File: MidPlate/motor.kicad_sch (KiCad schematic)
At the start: 3 parts, among them J13 JST_BM04B-GHS-TBT, J7 430450818, J8 Molex_43045_8pinMicrofit

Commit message: midplate changes, ready for order
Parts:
- removed J8: Molex_43045_8pinMicrofit, bots:Molex_Micro-Fit_3.0_43045-0812_2x04_P3.00mm_Vertical, symbol bots:Molex_43045_8pinMicrofit
- added JP1: Jumper_2_Bridged, Connector_PinHeader_2.54mm:PinHeader_1x02_P2.54mm_Vertical, symbol Jumper:Jumper_2_Bridged
- added R3: R_110R, bots:R_0603_1608Metric, symbol bots:R_110R
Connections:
- net CAN+: now also R3.2
- net CAN-: now also JP1.1 (A)
- new net: JP1.2 (B), R3.1
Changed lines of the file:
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@@
 (kicad_sch (version 20230121) (generator eeschema)
   (paper "A4")
-  (junction (at 189.23 40.64) (diameter 0) (color 0 0 0 0)
-  )
   (junction (at 170.18 60.96) (diameter 0) (color 0 0 0 0)
   )
   (junction (at 195.58 66.04) (diameter 0) (color 0 0 0 0)
   )
+  (junction (at 118.11 110.49) (diameter 0) (color 0 0 0 0)
+  )
+  (junction (at 92.71 110.49) (diameter 0) (color 0 0 0 0)
+  )
   (junction (at 195.58 63.5) (diameter 0) (color 0 0 0 0)
   )
-  (junction (at 176.53 45.72) (diameter 0) (color 0 0 0 0)
-  )
-  (junction (at 176.53 43.18) (diameter 0) (color 0 0 0 0)
-  )
-  (junction (at 189.23 43.18) (diameter 0) (color 0 0 0 0)
-  )
-  (junction (at 176.53 40.64) (diameter 0) (color 0 0 0 0)
-  )
-  (junction (at 189.23 45.72) (diameter 0) (color 0 0 0 0)
-  )
   (junction (at 170.18 63.5) (diameter 0) (color 0 0 0 0)
   )
@@
     (stroke (width 0) (type default))
   )
-  (wire (pts (xy 189.23 52.07) (xy 195.58 52.07))
-    (stroke (width 0) (type default))
-  )
-  (wire (pts (xy 176.53 43.18) (xy 176.53 45.72))
-    (stroke (width 0) (type default))
-  )
   (wire (pts (xy 107.95 80.01) (xy 107.95 87.63))
     (stroke (width 0) (type default))
   )
-  (wire (pts (xy 170.18 53.34) (xy 170.18 60.96))
-    (stroke (width 0) (type default))
-  )
-  (wire (pts (xy 189.23 40.64) (xy 189.23 43.18))
-    (stroke (width 0) (type default))
-  )
-  (wire (pts (xy 176.53 40.64) (xy 176.53 43.18))
+  (wire (pts (xy 92.71 106.68) (xy 113.03 106.68))
+    (stroke (width 0) (type default))
+  )
+  (wire (pts (xy 105.41 110.49) (xy 107.95 110.49))
     (stroke (width 0) (type default))
   )
@@
     (stroke (width 0) (type default))
   )
+  (wire (pts (xy 92.71 106.68) (xy 92.71 110.49))
+    (stroke (width 0) (type default))
+  )
   (wire (pts (xy 161.29 68.58) (xy 161.29 60.96))
     (stroke (width 0) (type default))
@@
     (stroke (width 0) (type default))
   )
-  (wire (pts (xy 115.57 72.39) (xy 115.57 80.01))
-    (stroke (width 0) (type default))
-  )
-  (wire (pts (xy 176.53 53.34) (xy 170.18 53.34))
+  (wire (pts (xy 118.11 106.68) (xy 118.11 110.49))
+    (stroke (width 0) (type default))
+  )
+  (wire (pts (xy 118.11 110.49) (xy 127 110.49))
     (stroke (width 0) (type default))
   )
@@
     (stroke (width 0) (type default))
   )
+  (wire (pts (xy 115.57 106.68) (xy 115.57 72.39))
+    (stroke (width 0) (type default))
+  )
   (wire (pts (xy 170.18 63.5) (xy 170.18 66.04))
     (stroke (width 0) (type default))
   )
+  (wire (pts (xy 118.11 106.68) (xy 115.57 106.68))
+    (stroke (width 0) (type default))
+  )
   (wire (pts (xy 120.65 80.01) (xy 120.65 88.9))
     (stroke (width 0) (type default))
   )
-  (wire (pts (xy 195.58 52.07) (xy 195.58 60.96))
+  (wire (pts (xy 88.9 110.49) (xy 92.71 110.49))
+    (stroke (width 0) (type default))
+  )
+  (wire (pts (xy 92.71 110.49) (xy 95.25 110.49))
     (stroke (width 0) (type default))
   )
@@
     (stroke (width 0) (type default))
   )
-  (wire (pts (xy 113.03 72.39) (xy 113.03 80.01))
-    (stroke (width 0) (type default))
-  )
-  (wire (pts (xy 189.23 43.18) (xy 189.23 45.72))
+  (wire (pts (xy 115.57 110.49) (xy 118.11 110.49))
     (stroke (width 0) (type default))
   )
@@
     (stroke (width 0) (type default))
   )
+  (wire (pts (xy 88.9 113.03) (xy 88.9 110.49))
+    (stroke (width 0) (type default))
+  )
   (wire (pts (xy 195.58 66.04) (xy 195.58 68.58))
     (stroke (width 0) (type default))
@@
     (stroke (width 0) (type default))
   )
-  (wire (pts (xy 176.53 45.72) (xy 176.53 53.34))
-    (stroke (width 0) (type default))
-  )
-  (wire (pts (xy 189.23 45.72) (xy 189.23 52.07))
-    (stroke (width 0) (type default))
-  )
-  (wire (pts (xy 189.23 38.1) (xy 189.23 40.64))
-    (stroke (width 0) (type default))
-  )
-  (wire (pts (xy 176.53 38.1) (xy 176.53 40.64))
-    (stroke (width 0) (type default))
-  )
-  (global_label "CAN+" (shape input) (at 115.57 80.01 270) (fields_autoplaced)
+  (wire (pts (xy 113.03 106.68) (xy 113.03 72.39))
+    (stroke (width 0) (type default))
+  )
+  (global_label "CAN+" (shape input) (at 127 110.49 270) (fields_autoplaced)
     (effects (font (size 1.27 1.27)) (justify right))
-    (property "Intersheetrefs" "${INTERSHEET_REFS}" (at 115.57 88.2567 90)
+    (property "Intersheetrefs" "${INTERSHEET_REFS}" (at 127 118.7367 90)
       (effects (font (size 1.27 1.27)) (justify right) hide)
     )
   )
-  (global_label "CAN-" (shape input) (at 113.03 80.01 270) (fields_autoplaced)
+  (global_label "CAN-" (shape input) (at 88.9 113.03 270) (fields_autoplaced)
     (effects (font (size 1.27 1.27)) (justify right))
-    (property "Intersheetrefs" "${INTERSHEET_REFS}" (at 113.03 88.2567 90)
+    (property "Intersheetrefs" "${INTERSHEET_REFS}" (at 88.9 121.2767 90)
       (effects (font (size 1.27 1.27)) (justify right) hide)
+    )
+  )
+  (symbol (lib_id "Jumper:Jumper_2_Bridged") (at 100.33 110.49 0) (unit 1)
+    (in_bom yes) (on_board yes) (dnp no)
+    (property "Reference" "JP1" (at 100.33 113.03 0)
+      (effects (font (size 1.27 1.27)))
+    )
+    (property "Value" "Jumper_2_Bridged" (at 100.33 107.95 0)
+      (effects (font (size 1.27 1.27)))
+    )
+    (property "Footprint" "Connector_PinHeader_2.54mm:PinHeader_1x02_P2.54mm_Vertical" (at 100.33 110.49 0)
+      (effects (font (size 1.27 1.27)) hide)
+    )
+    (property "Datasheet" "~" (at 100.33 110.49 0)
+      (effects (font (size 1.27 1.27)) hide)
+    )
+    (pin "1")
+    (pin "2")
+    (instances
+      (project "midplate"
+        (path "/69058343-dac8-421b-a3f6-e069eb1ba8ae/dd4f1e83-2671-4cd9-8990-217fc355ed24"
+          (reference "JP1") (unit 1)
+        )
+        (path "/69058343-dac8-421b-a3f6-e069eb1ba8ae/5956ea5b-5c98-49b4-b8ae-cf424631ffad"
+          (reference "JP1") (unit 1)
+        )
+      )
+    )
+  )
+  (symbol (lib_id "bots:R_110R") (at 111.76 110.49 90) (unit 1)
+    (in_bom yes) (on_board yes) (dnp no)
+    (property "Reference" "R3" (at 110.49 113.03 90)
+      (effects (font (size 1.27 1.27)))
+    )
+    (property "Value" "R_110R" (at 113.03 107.95 90)
+      (effects (font (size 1.27 1.27)))
+    )
+    (property "Footprint" "bots:R_0603_1608Metric" (at 111.76 112.268 90)
+      (effects (font (size 1.27 1.27)) hide)
+    )
+    (property "Datasheet" "~" (at 111.76 110.49 0)
+      (effects (font (size 1.27 1.27)) hide)
+    )
+    (property "MPN" "0603WAF1100T5E" (at 111.76 110.49 0)
+      (effects (font (size 1.27 1.27)) hide)
+    )
+    (property "Manufacturer" "UNI-ROYAL(Uniroyal Elec)" (at 111.76 110.49 0)
+      (effects (font (size 1.27 1.27)) hide)
+    )
+    (property "Price" "0.001" (at 111.76 110.49 0)
+      (effects (font (size 1.27 1.27)) hide)
+    )
+    (property "JLC" "0603" (at 111.76 110.49 0)
+      (effects (font (size 1.27 1.27)) hide)
+    )
+    (property "LCSC" "C22781" (at 111.76 110.49 0)
+      (effects (font (size 1.27 1.27)) hide)
+    )
+    (pin "1")
+    (pin "2")
+    (instances
+      (project "midplate"
+        (path "/69058343-dac8-421b-a3f6-e069eb1ba8ae/5956ea5b-5c98-49b4-b8ae-cf424631ffad"
+          (reference "R3") (unit 1)
+        )
+      )
     )
   )
@@
         )
       )
-    )
-  )
-  (symbol (lib_id "bots:Molex_43045_8pinMicrofit") (at 181.61 40.64 0) (unit 1)
-    (in_bom yes) (on_board yes) (dnp no) (fields_autoplaced)
-    (property "Reference" "J8" (at 182.88 31.75 0)
-      (effects (font (size 1.27 1.27)))
-    )
-    (property "Value" "Molex_43045_8pinMicrofit" (at 182.88 34.29 0)
-      (effects (font (size 1.27 1.27)))
-    )
-    (property "Footprint" "bots:Molex_Micro-Fit_3.0_43045-0812_2x04_P3.00mm_Vertical" (at 181.61 40.64 0)
-      (effects (font (size 1.27 1.27)) hide)
-    )
-    (property "Datasheet" "~" (at 181.61 40.64 0)
-      (effects (font (size 1.27 1.27)) hide)
-    )
-    (pin "1")
-    (pin "2")
-    (pin "3")
-    (pin "4")
-    (pin "5")
-    (pin "6")
-    (pin "7")
-    (pin "8")
-    (instances
-      (project "midplate"
-        (path "/69058343-dac8-421b-a3f6-e069eb1ba8ae/5956ea5b-5c98-49b4-b8ae-cf424631ffad"
-          (reference "J8") (unit 1)
-        )
-      )

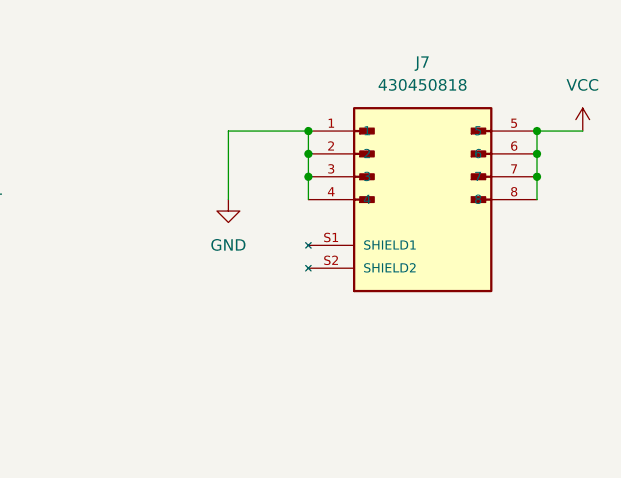
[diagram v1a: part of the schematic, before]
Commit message: midplate updates
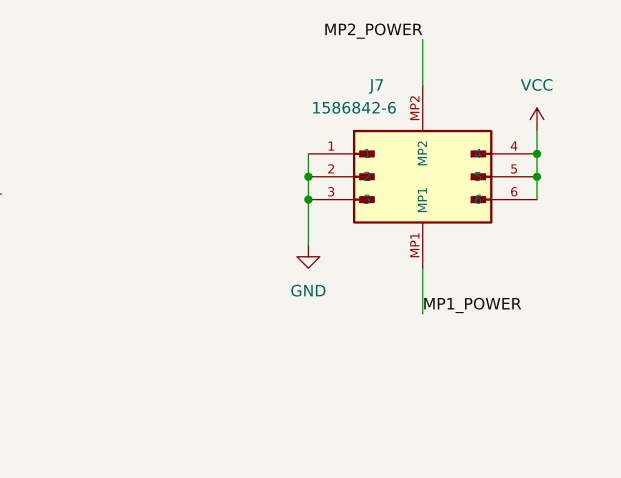
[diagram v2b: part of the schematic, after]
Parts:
- removed J7: 430450818, bots:MOLEX_430450818, symbol bots:MOLEX_430450818
- added J7: 1586842-6, bots:TE_1586842-6_6PIN, symbol bots:TE_1586842-6_6PIN
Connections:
- net GND: now also J7.1, J7.2, J7.3
- net VCC: now also J7.4, J7.5, J7.6
- new net MP1_POWER: J7.MP1
- new net MP2_POWER: J7.MP2

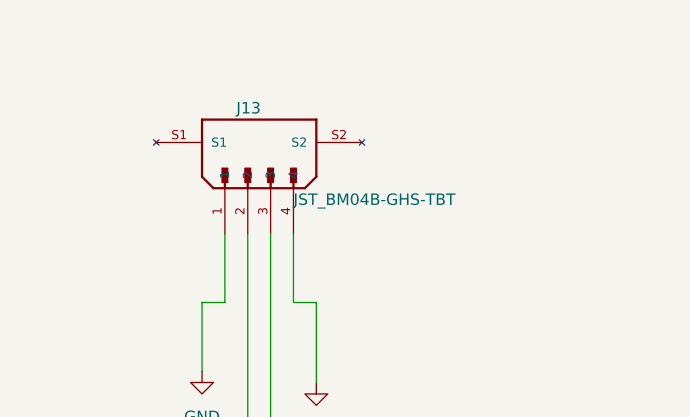
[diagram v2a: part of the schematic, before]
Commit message: midplate 5V buck converter
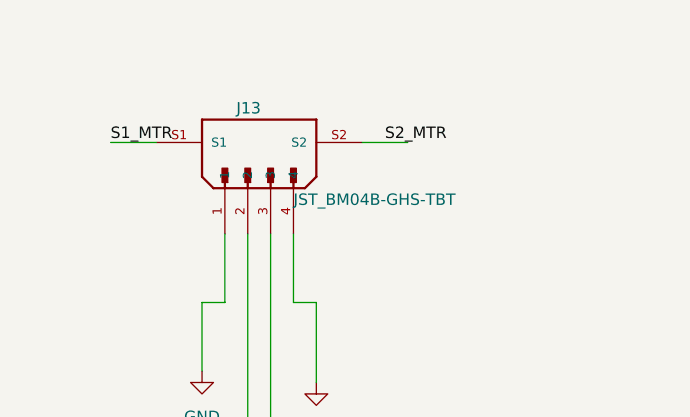
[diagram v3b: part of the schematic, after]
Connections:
- net S1_MTR: now reaches J13.S1
- net S2_MTR: now reaches J13.S2
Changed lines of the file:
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@@
+    (stroke (width 0) (type default))
+  )
+  (wire (pts (xy 97.79 62.23) (xy 102.87 62.23))
     (stroke (width 0) (type default))
   )
@@
   )
   (wire (pts (xy 118.11 110.49) (xy 127 110.49))
+    (stroke (width 0) (type default))
+  )
+  (wire (pts (xy 125.73 62.23) (xy 130.81 62.23))
     (stroke (width 0) (type default))
   )
@@
     (stroke (width 0) (type default))
   )
+  (label "S2_MTR" (at 128.27 62.23 0) (fields_autoplaced)
+    (effects (font (size 1.27 1.27)) (justify left bottom))
+  )
   (label "MP2_POWER" (at 182.88 50.8 180) (fields_autoplaced)
     (effects (font (size 1.27 1.27)) (justify right bottom))
   )
+  (label "S1_MTR" (at 97.79 62.23 0) (fields_autoplaced)
+    (effects (font (size 1.27 1.27)) (justify left bottom))
+  )
   (label "MP1_POWER" (at 182.88 81.28 0) (fields_autoplaced)

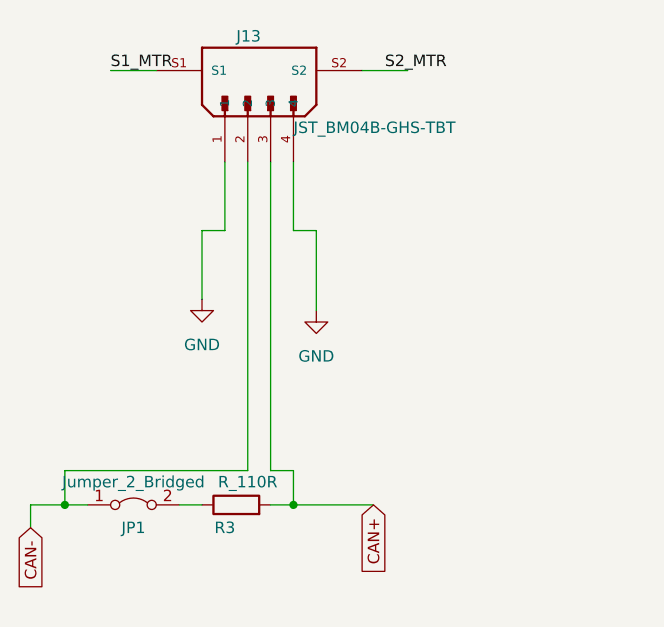
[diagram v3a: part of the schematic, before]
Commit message: swapped pins around for CAN
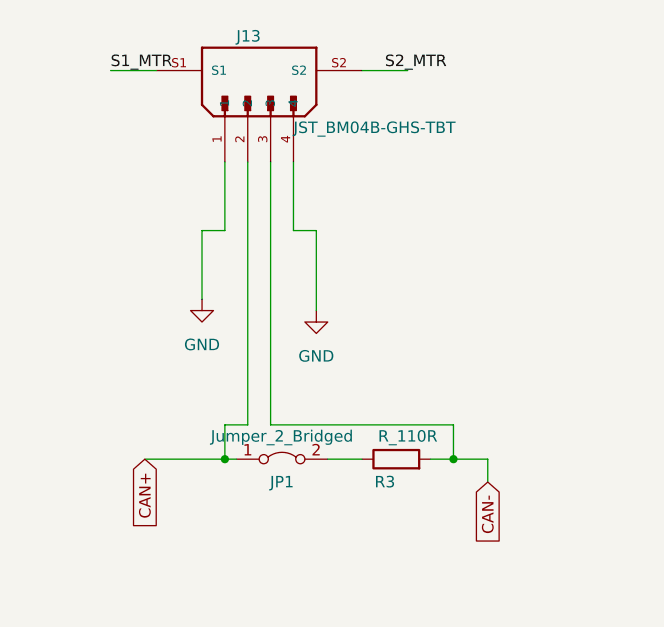
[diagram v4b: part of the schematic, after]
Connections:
- net CAN+: now also J13.2, JP1.1 (A); no longer J13.3, R3.2
- net CAN-: now also J13.3, R3.2; no longer J13.2, JP1.1 (A)
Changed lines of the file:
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@@
   (junction (at 170.18 66.04) (diameter 0) (color 0 0 0 0)
   )
-  (junction (at 118.11 110.49) (diameter 0) (color 0 0 0 0)
-  )
-  (junction (at 92.71 110.49) (diameter 0) (color 0 0 0 0)
+  (junction (at 110.49 105.41) (diameter 0) (color 0 0 0 0)
+  )
+  (junction (at 135.89 105.41) (diameter 0) (color 0 0 0 0)
   )
   (junction (at 195.58 63.5) (diameter 0) (color 0 0 0 0)
@@
     (stroke (width 0) (type default))
   )
-  (wire (pts (xy 92.71 106.68) (xy 113.03 106.68))
-    (stroke (width 0) (type default))
-  )
-  (wire (pts (xy 105.41 110.49) (xy 107.95 110.49))
-    (stroke (width 0) (type default))
-  )
-  (wire (pts (xy 92.71 106.68) (xy 92.71 110.49))
+  (wire (pts (xy 135.89 101.6) (xy 115.57 101.6))
+    (stroke (width 0) (type default))
+  )
+  (wire (pts (xy 121.92 105.41) (xy 125.73 105.41))
+    (stroke (width 0) (type default))
+  )
+  (wire (pts (xy 113.03 72.39) (xy 113.03 101.6))
+    (stroke (width 0) (type default))
+  )
+  (wire (pts (xy 135.89 101.6) (xy 135.89 105.41))
     (stroke (width 0) (type default))
   )
@@
     (stroke (width 0) (type default))
   )
-  (wire (pts (xy 118.11 106.68) (xy 118.11 110.49))
-    (stroke (width 0) (type default))
-  )
-  (wire (pts (xy 118.11 110.49) (xy 127 110.49))
+  (wire (pts (xy 110.49 101.6) (xy 110.49 105.41))
+    (stroke (width 0) (type default))
+  )
+  (wire (pts (xy 110.49 105.41) (xy 101.6 105.41))
+    (stroke (width 0) (type default))
+  )
+  (wire (pts (xy 115.57 72.39) (xy 115.57 101.6))
     (stroke (width 0) (type default))
   )
@@
     (stroke (width 0) (type default))
   )
-  (wire (pts (xy 115.57 106.68) (xy 115.57 72.39))
-    (stroke (width 0) (type default))
-  )
-  (wire (pts (xy 118.11 106.68) (xy 115.57 106.68))
+  (wire (pts (xy 110.49 101.6) (xy 113.03 101.6))
     (stroke (width 0) (type default))
   )
@@
     (stroke (width 0) (type default))
   )
-  (wire (pts (xy 88.9 110.49) (xy 92.71 110.49))
-    (stroke (width 0) (type default))
-  )
-  (wire (pts (xy 92.71 110.49) (xy 95.25 110.49))
-    (stroke (width 0) (type default))
-  )
-  (wire (pts (xy 115.57 110.49) (xy 118.11 110.49))
+  (wire (pts (xy 139.7 105.41) (xy 135.89 105.41))
+    (stroke (width 0) (type default))
+  )
+  (wire (pts (xy 135.89 105.41) (xy 133.35 105.41))
+    (stroke (width 0) (type default))
+  )
+  (wire (pts (xy 111.76 105.41) (xy 110.49 105.41))
     (stroke (width 0) (type default))
   )
@@
     (stroke (width 0) (type default))
   )
-  (wire (pts (xy 88.9 113.03) (xy 88.9 110.49))
+  (wire (pts (xy 139.7 107.95) (xy 139.7 105.41))
     (stroke (width 0) (type default))
   )
@@
   )
   (wire (pts (xy 170.18 63.5) (xy 170.18 66.04))
-    (stroke (width 0) (type default))
-  )
-  (wire (pts (xy 113.03 106.68) (xy 113.03 72.39))
     (stroke (width 0) (type default))
   )
@@
     (effects (font (size 1.27 1.27)) (justify left bottom))
   )
-  (global_label "CAN+" (shape input) (at 127 110.49 270) (fields_autoplaced)
+  (global_label "CAN+" (shape input) (at 101.6 105.41 270) (fields_autoplaced)
     (effects (font (size 1.27 1.27)) (justify right))
-    (property "Intersheetrefs" "${INTERSHEET_REFS}" (at 127 118.7367 90)
-      (effects (font (size 1.27 1.27)) (justify right) hide)
-    )
-  )
-  (global_label "CAN-" (shape input) (at 88.9 113.03 270) (fields_autoplaced)
+    (property "Intersheetrefs" "${INTERSHEET_REFS}" (at 101.6 113.6567 90)
+      (effects (font (size 1.27 1.27)) (justify left) hide)
+    )
+  )
+  (global_label "CAN-" (shape input) (at 139.7 107.95 270) (fields_autoplaced)
     (effects (font (size 1.27 1.27)) (justify right))
-    (property "Intersheetrefs" "${INTERSHEET_REFS}" (at 88.9 121.2767 90)
-      (effects (font (size 1.27 1.27)) (justify right) hide)
-    )
-  )
-  (symbol (lib_id "Jumper:Jumper_2_Bridged") (at 100.33 110.49 0) (unit 1)
+    (property "Intersheetrefs" "${INTERSHEET_REFS}" (at 139.7 116.1967 90)
+      (effects (font (size 1.27 1.27)) (justify left) hide)
+    )
+  )
+  (symbol (lib_id "Jumper:Jumper_2_Bridged") (at 116.84 105.41 0) (unit 1)
     (in_bom yes) (on_board yes) (dnp no)
-    (property "Reference" "JP1" (at 100.33 113.03 0)
-      (effects (font (size 1.27 1.27)))
-    )
-    (property "Value" "Jumper_2_Bridged" (at 100.33 107.95 0)
-      (effects (font (size 1.27 1.27)))
-    )
-    (property "Footprint" "Connector_PinHeader_2.54mm:PinHeader_1x02_P2.54mm_Vertical" (at 100.33 110.49 0)
-      (effects (font (size 1.27 1.27)) hide)
-    )
-    (property "Datasheet" "~" (at 100.33 110.49 0)
+    (property "Reference" "JP1" (at 116.84 107.95 0)
+      (effects (font (size 1.27 1.27)))
+    )
+    (property "Value" "Jumper_2_Bridged" (at 116.84 102.87 0)
+      (effects (font (size 1.27 1.27)))
+    )
+    (property "Footprint" "Connector_PinHeader_2.54mm:PinHeader_1x02_P2.54mm_Vertical" (at 116.84 105.41 0)
+      (effects (font (size 1.27 1.27)) hide)
+    )
+    (property "Datasheet" "~" (at 116.84 105.41 0)
       (effects (font (size 1.27 1.27)) hide)
     )
@@
     )
   )
-  (symbol (lib_id "bots:R_110R") (at 111.76 110.49 90) (unit 1)
-    (in_bom yes) (on_board yes) (dnp no)
-    (property "Reference" "R3" (at 110.49 113.03 90)
-      (effects (font (size 1.27 1.27)))
-    )
-    (property "Value" "R_110R" (at 113.03 107.95 90)
-      (effects (font (size 1.27 1.27)))
-    )
-    (property "Footprint" "bots:R_0603_1608Metric" (at 111.76 112.268 90)
-      (effects (font (size 1.27 1.27)) hide)
-    )
-    (property "Datasheet" "~" (at 111.76 110.49 0)
-      (effects (font (size 1.27 1.27)) hide)
-    )
-    (property "MPN" "0603WAF1100T5E" (at 111.76 110.49 0)
-      (effects (font (size 1.27 1.27)) hide)
-    )
-    (property "Manufacturer" "UNI-ROYAL(Uniroyal Elec)" (at 111.76 110.49 0)
-      (effects (font (size 1.27 1.27)) hide)
-    )
-    (property "Price" "0.001" (at 111.76 110.49 0)
-      (effects (font (size 1.27 1.27)) hide)
-    )
-    (property "JLC" "0603" (at 111.76 110.49 0)
-      (effects (font (size 1.27 1.27)) hide)
-    )
-    (property "LCSC" "C22781" (at 111.76 110.49 0)
-      (effects (font (size 1.27 1.27)) hide)
-    )
-    (pin "1")
-    (pin "2")
-    (instances
-      (project "midplate"
-        (path "/69058343-dac8-421b-a3f6-e069eb1ba8ae/5956ea5b-5c98-49b4-b8ae-cf424631ffad"
-          (reference "R3") (unit 1)
-        )
-      )
-    )
-  )
   (symbol (lib_id "power:GND") (at 107.95 87.63 0) (unit 1)
     (in_bom yes) (on_board yes) (dnp no) (fields_autoplaced)
@@
         )
       )
+    )
+  )
+  (symbol (lib_id "bots:R_110R") (at 129.54 105.41 90) (unit 1)
+    (in_bom yes) (on_board yes) (dnp no)
+    (property "Reference" "R3" (at 128.27 107.95 90)
+      (effects (font (size 1.27 1.27)))
+    )
+    (property "Value" "R_110R" (at 130.81 102.87 90)
+      (effects (font (size 1.27 1.27)))
+    )
+    (property "Footprint" "bots:R_0603_1608Metric" (at 129.54 107.188 90)
+      (effects (font (size 1.27 1.27)) hide)
+    )
+    (property "Datasheet" "~" (at 129.54 105.41 0)
+      (effects (font (size 1.27 1.27)) hide)
+    )
+    (property "MPN" "0603WAF1100T5E" (at 129.54 105.41 0)
+      (effects (font (size 1.27 1.27)) hide)
+    )
+    (property "Manufacturer" "UNI-ROYAL(Uniroyal Elec)" (at 129.54 105.41 0)
+      (effects (font (size 1.27 1.27)) hide)
+    )
+    (property "Price" "0.001" (at 129.54 105.41 0)
+      (effects (font (size 1.27 1.27)) hide)
+    )
+    (property "JLC" "0603" (at 129.54 105.41 0)
+      (effects (font (size 1.27 1.27)) hide)
+    )
+    (property "LCSC" "C22781" (at 129.54 105.41 0)
+      (effects (font (size 1.27 1.27)) hide)
+    )
+    (pin "1")
+    (pin "2")
+    (instances
+      (project "midplate"
+        (path "/69058343-dac8-421b-a3f6-e069eb1ba8ae/5956ea5b-5c98-49b4-b8ae-cf424631ffad"
+          (reference "R3") (unit 1)
+        )
+      )
